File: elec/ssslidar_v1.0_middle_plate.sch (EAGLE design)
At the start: 6 parts

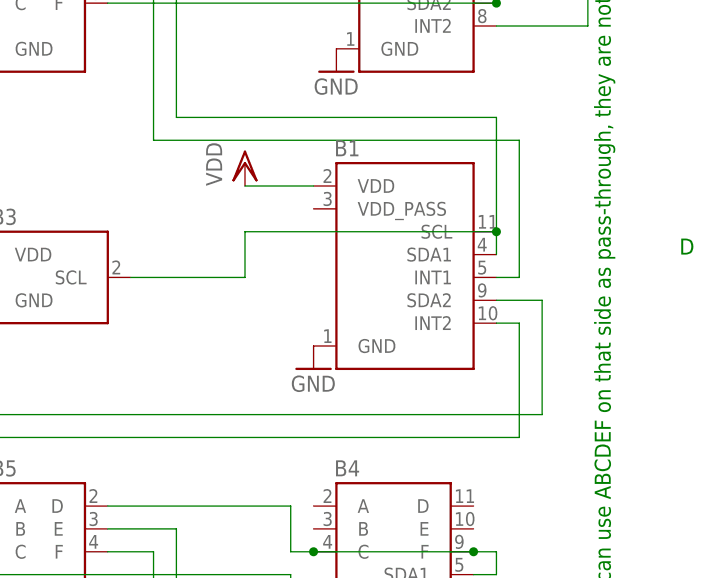
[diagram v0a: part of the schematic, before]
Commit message: Upadted blade footprint, put everything in v1.0
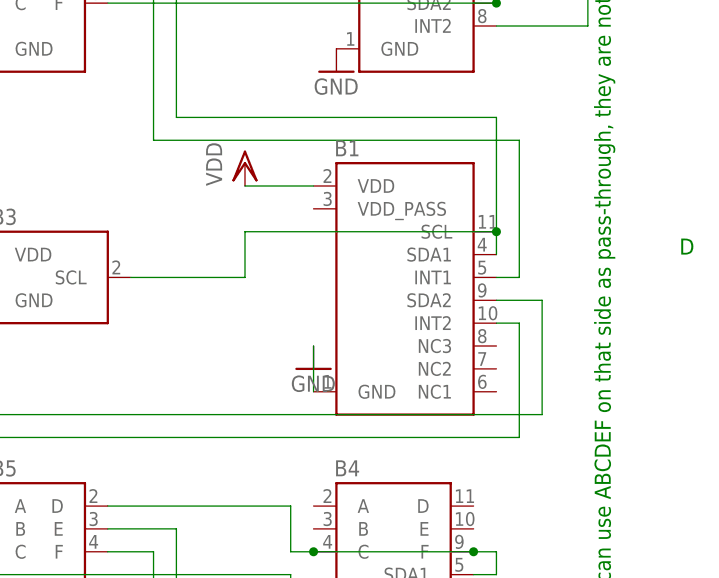
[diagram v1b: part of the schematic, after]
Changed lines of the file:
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@@
 <pinref part="B1" gate="G$1" pin="GND"/>
 <pinref part="GND2" gate="1" pin="GND"/>
+<wire x1="35.56" y1="60.96" x2="35.56" y2="55.88" width="0.1524" layer="91"/>
 </segment>
 <segment>
